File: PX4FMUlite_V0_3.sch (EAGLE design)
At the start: 151 parts, among them J2 DF13-4P-1.25V, J201 DF13C-6P-1.25V, J202 DF13C-6P-1.25V, J203 DF13C-6P-1.25V, J3 DF13C-4P-1.25V, J302 DF13C-4P-1.25V, J401 DF13C-4P-1.25V, J403 DF13C-7P-1.25V, J405 DF13C-4P-1.25V, J801 JST-ZH-3, J802 DF13C-3P-1.25V, M3_MOUNT1101 MOUNT-HOLE3.1MM, M3_MOUNT1102 MOUNT-HOLE3.1MM, M3_MOUNT1103 MOUNT-HOLE3.1MM, M3_MOUNT1104 MOUNT-HOLE3.1MM, U101 STM32F4X7VX, U2 MAX3051, U401 MAX3051, U903 74LVC2G240, X101 3.2x2.5 mm / 24 MHz / 15 ppm

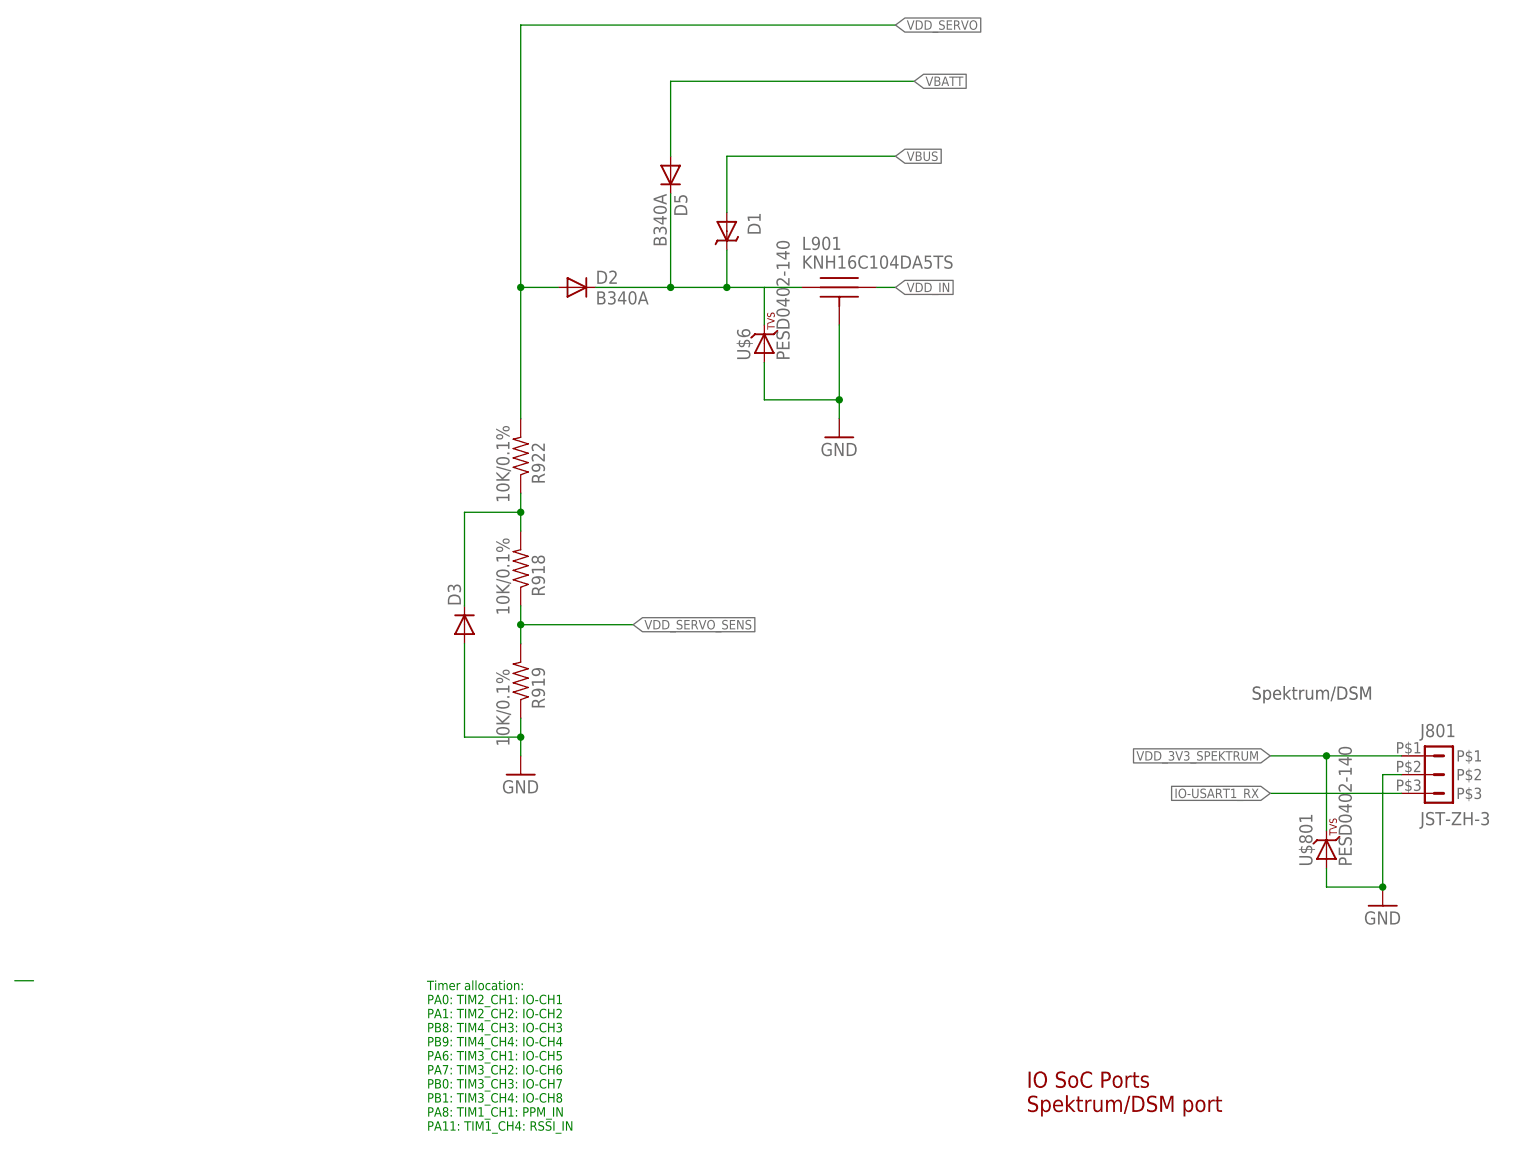
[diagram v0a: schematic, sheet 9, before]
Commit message: buck-boost half wired. CAN wiring in progress.
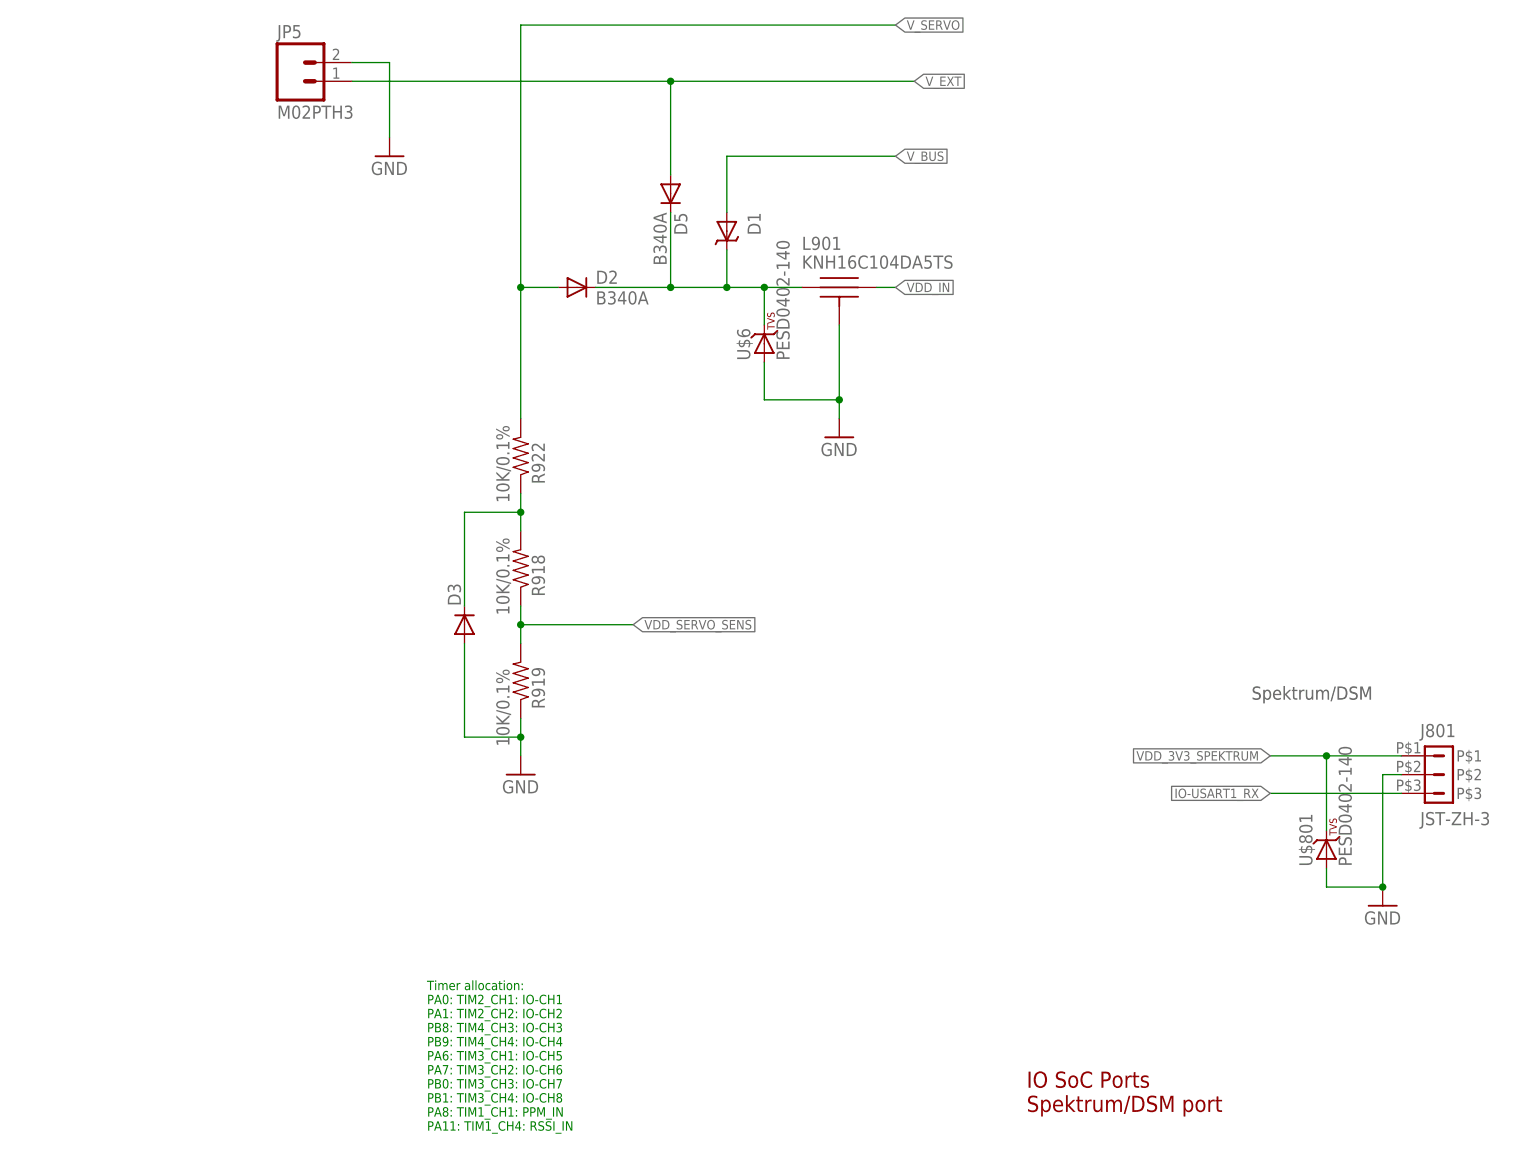
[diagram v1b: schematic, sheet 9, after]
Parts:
- added JP5: M02PTH3, SparkFun-Connectors:M02PTH3
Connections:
- net VBUS renamed V_BUS
- net VDD_SERVO renamed V_SERVO
- removed net N$14: C1.2, C10.2, C8.2, C9.2, U$15.PGND
- removed net VBATT: D5.A
- removed net VOUT: C10.1, C8.1, C9.1, U$15.VOUT
- new net V_EXT: D5.A, JP5.1
- net FMU-BOOT0: now also FMU-BOOT1101.P$1
- net GND: now also C1.2, C10.2, C8.2, C9.2, JP5.2, U$15.PGND
- net GYRO_DRDY: now also U$2.INT2
- net VDD_5V_IN: now also C10.1, C8.1, C9.1, U$15.VOUT
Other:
- moved on the sheet: D5, J1-VCC
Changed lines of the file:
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@@
 <part name="C10" library="SparkFun-Capacitors" deviceset="22UF-16V-20%-(1210)" device="" value="22uF"/>
 <part name="C1" library="SparkFun-Capacitors" deviceset="22UF-16V-20%-(1210)" device="" value="22uF"/>
+<part name="JP5" library="SparkFun-Connectors" deviceset="M02" device="PTH3"/>
+<part name="GND18" library="pixhawk2" deviceset="GND" device=""/>
 </parts>
 <sheets>
@@
 </segment>
 </net>
-<net name="VBUS" class="1">
+<net name="V_BUS" class="1">
 <segment>
 <pinref part="U101" gate="PORTA_H" pin="PA9"/>
@@
 </segment>
 </net>
-<net name="VBUS" class="1">
+<net name="V_BUS" class="1">
 <segment>
 <wire x1="76.2" y1="152.4" x2="76.2" y2="134.62" width="0.1524" layer="91"/>
@@
 <instances>
 <instance part="FRAME3" gate="G$1" x="0" y="0"/>
-<instance part="GND23" gate="1" x="81.28" y="33.02"/>
+<instance part="GND23" gate="1" x="81.28" y="30.48"/>
 <instance part="C508" gate="G$1" x="81.28" y="83.82">
 <attribute name="PARTNO" x="81.28" y="83.82" size="1.778" layer="96" display="off"/>
@@
 <pinref part="C508" gate="G$1" pin="2"/>
 <pinref part="U$2" gate="A" pin="GND"/>
-<wire x1="81.28" y1="40.64" x2="81.28" y2="35.56" width="0.1524" layer="91"/>
+<wire x1="81.28" y1="40.64" x2="81.28" y2="33.02" width="0.1524" layer="91"/>
 <wire x1="116.84" y1="45.72" x2="116.84" y2="40.64" width="0.1524" layer="91"/>
 <wire x1="116.84" y1="40.64" x2="101.6" y2="40.64" width="0.1524" layer="91"/>
@@
 <label x="147.32" y="60.96" size="1.27" layer="95" rot="MR180" xref="yes"/>
 <wire x1="129.54" y1="60.96" x2="147.32" y2="60.96" width="0.1524" layer="91"/>
+<pinref part="U$2" gate="A" pin="INT2"/>
 </segment>
 </net>
@@
 </busses>
 <nets>
-<net name="VDD_5V_IN" class="1">
-<segment>
-<wire x1="213.36" y1="124.46" x2="233.68" y2="124.46" width="0.1524" layer="91"/>
-<label x="233.68" y="124.46" size="1.27" layer="95" xref="yes"/>
-</segment>
-</net>
 <net name="!VDD_SERVO_VALID" class="0">
 <segment>
@@
 <pinref part="U$15" gate="A" pin="GND"/>
 <pinref part="SUPPLY2" gate="GND" pin="GND"/>
-<wire x1="93.98" y1="66.04" x2="93.98" y2="88.9" width="0.1524" layer="91"/>
+<wire x1="93.98" y1="66.04" x2="93.98" y2="71.12" width="0.1524" layer="91"/>
+<pinref part="U$15" gate="A" pin="PGND"/>
+<wire x1="93.98" y1="71.12" x2="93.98" y2="88.9" width="0.1524" layer="91"/>
+<wire x1="109.22" y1="88.9" x2="109.22" y2="83.82" width="0.1524" layer="91"/>
+<wire x1="109.22" y1="83.82" x2="101.6" y2="83.82" width="0.1524" layer="91"/>
+<wire x1="101.6" y1="83.82" x2="40.64" y2="83.82" width="0.1524" layer="91"/>
+<wire x1="40.64" y1="106.68" x2="40.64" y2="83.82" width="0.1524" layer="91"/>
+<pinref part="C8" gate="G$1" pin="2"/>
+<wire x1="109.22" y1="83.82" x2="147.32" y2="83.82" width="0.1524" layer="91"/>
+<wire x1="147.32" y1="83.82" x2="157.48" y2="83.82" width="0.1524" layer="91"/>
+<wire x1="157.48" y1="83.82" x2="170.18" y2="83.82" width="0.1524" layer="91"/>
+<wire x1="170.18" y1="83.82" x2="170.18" y2="109.22" width="0.1524" layer="91"/>
+<pinref part="C10" gate="G$1" pin="2"/>
+<wire x1="157.48" y1="109.22" x2="157.48" y2="83.82" width="0.1524" layer="91"/>
+<pinref part="C9" gate="G$1" pin="2"/>
+<wire x1="147.32" y1="109.22" x2="147.32" y2="83.82" width="0.1524" layer="91"/>
+<junction x="147.32" y="83.82"/>
+<junction x="157.48" y="83.82"/>
+<pinref part="C1" gate="G$1" pin="2"/>
+<junction x="109.22" y="83.82"/>
+<wire x1="101.6" y1="83.82" x2="101.6" y2="71.12" width="0.1524" layer="91"/>
+<wire x1="101.6" y1="71.12" x2="93.98" y2="71.12" width="0.1524" layer="91"/>
+<junction x="93.98" y="71.12"/>
 </segment>
 </net>
 <net name="VDD_IN" class="1">
 <segment>
-<label x="20.32" y="124.46" size="1.27" layer="95" rot="R180" xref="yes"/>
+<label x="22.86" y="124.46" size="1.27" layer="95" rot="R180" xref="yes"/>
 <pinref part="U$15" gate="A" pin="VIN"/>
 <pinref part="U$15" gate="A" pin="EN"/>
-<wire x1="20.32" y1="124.46" x2="40.64" y2="124.46" width="0.1524" layer="91"/>
+<wire x1="22.86" y1="124.46" x2="40.64" y2="124.46" width="0.1524" layer="91"/>
 <wire x1="40.64" y1="124.46" x2="76.2" y2="124.46" width="0.1524" layer="91"/>
 <wire x1="76.2" y1="124.46" x2="81.28" y2="124.46" width="0.1524" layer="91"/>
@@
 <wire x1="40.64" y1="114.3" x2="40.64" y2="124.46" width="0.1524" layer="91"/>
 <pinref part="C1" gate="G$1" pin="1"/>
+<junction x="40.64" y="124.46"/>
 </segment>
 </net>
@@
 </segment>
 </net>
-<net name="N$14" class="0">
-<segment>
-<pinref part="U$15" gate="A" pin="PGND"/>
-<wire x1="109.22" y1="88.9" x2="109.22" y2="83.82" width="0.1524" layer="91"/>
-<wire x1="109.22" y1="83.82" x2="40.64" y2="83.82" width="0.1524" layer="91"/>
-<wire x1="40.64" y1="106.68" x2="40.64" y2="83.82" width="0.1524" layer="91"/>
-<pinref part="C8" gate="G$1" pin="2"/>
-<wire x1="109.22" y1="83.82" x2="147.32" y2="83.82" width="0.1524" layer="91"/>
-<wire x1="147.32" y1="83.82" x2="157.48" y2="83.82" width="0.1524" layer="91"/>
-<wire x1="157.48" y1="83.82" x2="170.18" y2="83.82" width="0.1524" layer="91"/>
-<wire x1="170.18" y1="83.82" x2="170.18" y2="109.22" width="0.1524" layer="91"/>
-<pinref part="C10" gate="G$1" pin="2"/>
-<wire x1="157.48" y1="109.22" x2="157.48" y2="83.82" width="0.1524" layer="91"/>
-<pinref part="C9" gate="G$1" pin="2"/>
-<wire x1="147.32" y1="109.22" x2="147.32" y2="83.82" width="0.1524" layer="91"/>
-<junction x="147.32" y="83.82"/>
-<junction x="157.48" y="83.82"/>
-<pinref part="C1" gate="G$1" pin="2"/>
-</segment>
-</net>
-<net name="VOUT" class="0">
+<net name="VDD_5V_IN" class="1">
 <segment>
 <pinref part="U$15" gate="A" pin="VOUT"/>
@@
 <pinref part="C9" gate="G$1" pin="1"/>
 <wire x1="147.32" y1="116.84" x2="147.32" y2="121.92" width="0.1524" layer="91"/>
+<wire x1="170.18" y1="121.92" x2="190.5" y2="121.92" width="0.1524" layer="91"/>
+<label x="190.5" y="121.92" size="1.27" layer="95" xref="yes"/>
+<junction x="170.18" y="121.92"/>
+<junction x="147.32" y="121.92"/>
+<junction x="157.48" y="121.92"/>
 </segment>
 </net>
@@
 <instance part="D3" gate="G$1" x="88.9" y="81.28" rot="R90"/>
 <instance part="D2" gate="G$1" x="104.14" y="127"/>
-<instance part="D5" gate="G$1" x="116.84" y="142.24" rot="R270"/>
+<instance part="D5" gate="G$1" x="116.84" y="139.7" rot="R270"/>
+<instance part="JP5" gate="G$1" x="66.04" y="154.94"/>
+<instance part="GND18" gate="1" x="78.74" y="144.78"/>
 </instances>
 <busses>
@@
 <junction x="96.52" y="66.04"/>
 </segment>
+<segment>
+<pinref part="JP5" gate="G$1" pin="2"/>
+<wire x1="73.66" y1="157.48" x2="78.74" y2="157.48" width="0.1524" layer="91"/>
+<wire x1="78.74" y1="157.48" x2="78.74" y2="147.32" width="0.1524" layer="91"/>
+<pinref part="GND18" gate="1" pin="GND"/>
+</segment>
 </net>
 <net name="IO-USART1_RX" class="0">
@@
 </segment>
 </net>
-<net name="IO-BOOT0" class="0">
-<segment>
-<wire x1="27.94" y1="33.02" x2="30.48" y2="33.02" width="0.1524" layer="91"/>
-</segment>
-</net>
 <net name="VDD_3V3_SPEKTRUM" class="1">
 <segment>
@@
 </segment>
 </net>
-<net name="VDD_SERVO" class="1">
+<net name="V_SERVO" class="1">
 <segment>
 <pinref part="R922" gate="G$1" pin="2"/>
@@
 </segment>
 </net>
-<net name="VBUS" class="1">
+<net name="V_BUS" class="1">
 <segment>
 <label x="147.32" y="144.78" size="1.27" layer="95" xref="yes"/>
@@
 <junction x="124.46" y="127"/>
 <pinref part="D5" gate="G$1" pin="C"/>
-<wire x1="116.84" y1="139.7" x2="116.84" y2="127" width="0.1524" layer="91"/>
+<wire x1="116.84" y1="137.16" x2="116.84" y2="127" width="0.1524" layer="91"/>
 <junction x="116.84" y="127"/>
+<junction x="129.54" y="127"/>
 </segment>
 </net>
-<net name="VBATT" class="1">
+<net name="V_EXT" class="1">
 <segment>
 <label x="149.86" y="154.94" size="1.27" layer="95" xref="yes"/>
 <wire x1="116.84" y1="154.94" x2="149.86" y2="154.94" width="0.1524" layer="91"/>
 <pinref part="D5" gate="G$1" pin="A"/>
-<wire x1="116.84" y1="154.94" x2="116.84" y2="144.78" width="0.1524" layer="91"/>
+<wire x1="116.84" y1="154.94" x2="116.84" y2="142.24" width="0.1524" layer="91"/>
+<pinref part="JP5" gate="G$1" pin="1"/>
+<wire x1="73.66" y1="154.94" x2="116.84" y2="154.94" width="0.1524" layer="91"/>
+<junction x="116.84" y="154.94"/>
 </segment>
 </net>
@@
 <instance part="J1" gate="-CH8" x="101.6" y="99.06"/>
 <instance part="J1" gate="-GND" x="63.5" y="83.82"/>
-<instance part="J1" gate="-VCC" x="71.12" y="152.4"/>
+<instance part="J1" gate="-VCC" x="66.04" y="152.4"/>
 <instance part="U$14" gate="G$1" x="142.24" y="71.12"/>
 <instance part="JP4" gate="G$1" x="165.1" y="45.72" rot="R90"/>
@@
 </segment>
 </net>
-<net name="VDD_SERVO" class="1">
+<net name="V_SERVO" class="1">
 <segment>
 <label x="50.8" y="152.4" size="1.27" layer="95" rot="R180" xref="yes"/>
 <pinref part="J1" gate="-VCC" pin="S"/>
-<wire x1="68.58" y1="152.4" x2="50.8" y2="152.4" width="0.1524" layer="91"/>
+<wire x1="63.5" y1="152.4" x2="50.8" y2="152.4" width="0.1524" layer="91"/>
 </segment>
 </net>
@@
 </segment>
 </net>
+<net name="FMU-BOOT0" class="0">
+<segment>
+<wire x1="223.52" y1="160.02" x2="215.9" y2="160.02" width="0.1524" layer="91"/>
+<label x="215.9" y="160.02" size="1.27" layer="95" rot="R180" xref="yes"/>
+<pinref part="FMU-BOOT1101" gate="G$1" pin="P$1"/>
+</segment>
+</net>
